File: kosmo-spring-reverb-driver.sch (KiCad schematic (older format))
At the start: 42 parts, among them Q1 BC639, Q2 BC640, U1 TL074

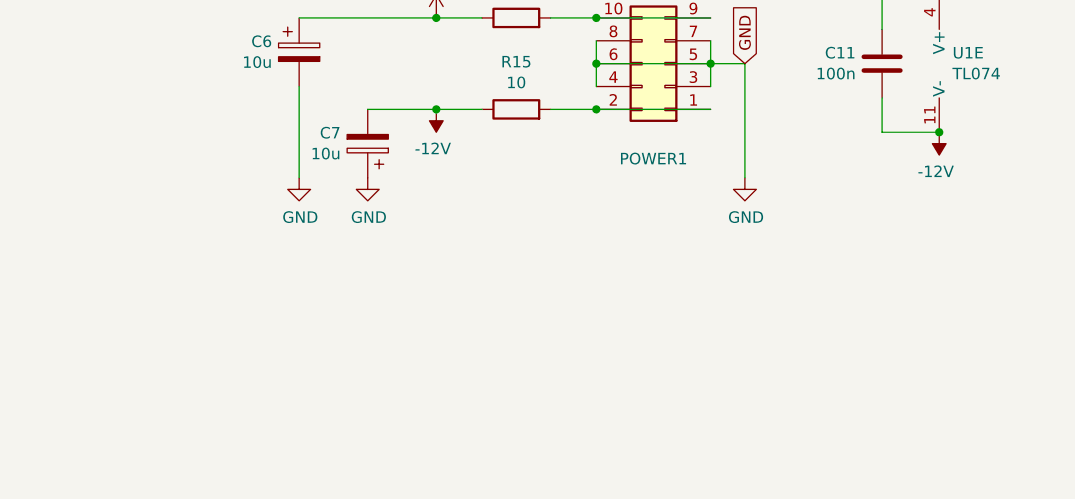
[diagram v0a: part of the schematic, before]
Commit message: Fix pot hole size, cap position
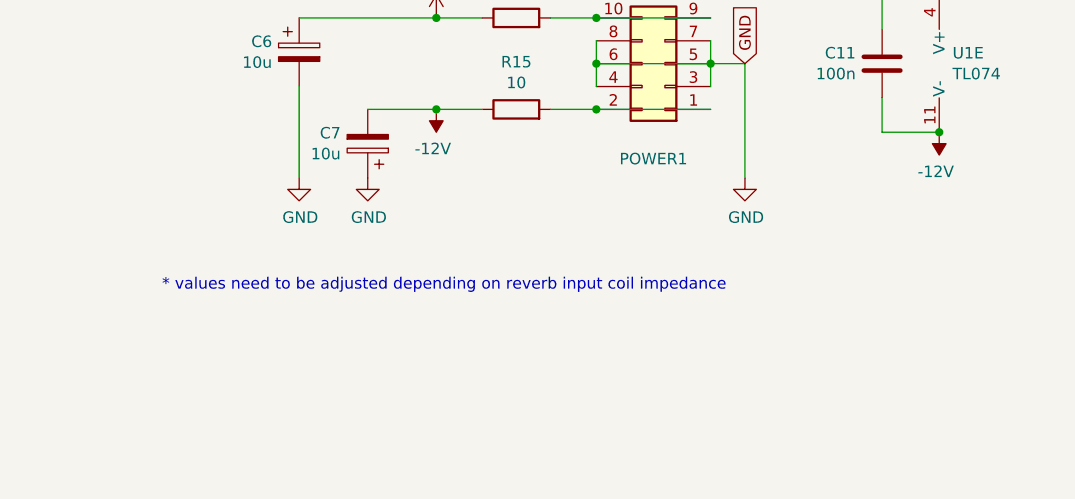
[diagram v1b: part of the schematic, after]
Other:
- note added: "* values need to be adjusted depending on reverb input coil impedance"
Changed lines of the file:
@@
 Title "Kosmo Spring Reverb Driver"
 Date "2021-02-17"
-Rev "v1.0.0"
+Rev "v1.0.1"
 Comp "Jan Knipper"
-Comment1 ""
+Comment1 "github.com/polykit/kosmo-spring-reverb-driver"
 Comment2 ""
 Comment3 ""
@@
 	9400 5250 8900 5250
 Connection ~ 8900 5250
+Text Notes 7000 6450 0    50   ~ 0
+* values need to be adjusted depending on reverb input coil impedance
 $EndSCHEMATC
